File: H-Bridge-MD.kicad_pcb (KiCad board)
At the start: 2 copper layers, 85 x 50 mm, 67 parts, among them IC1 SI8650AB-B-IS1, IC2 A3921KLPTR-T, IC3 SI8650AB-B-IS1, IC4 A3921KLPTR-T, J1 Conn_01x02, J2 Conn_01x03, J3 Conn_01x05, J4 Conn_01x02, J5 Bus_mechaken_PCIexpress_x16_1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, Q1 NVMFD5C446NT1G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

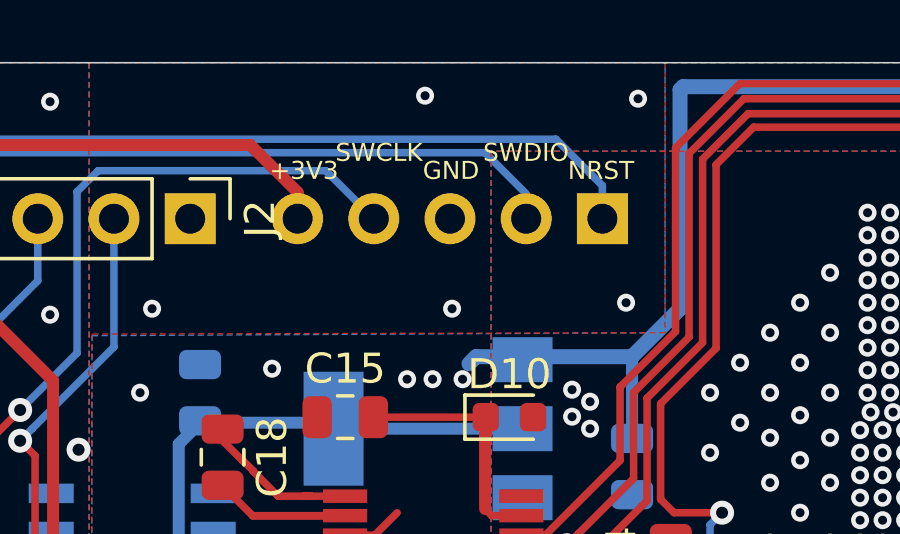
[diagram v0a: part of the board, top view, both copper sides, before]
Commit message: change
書き込み用のピンをコンスルー対応に変更
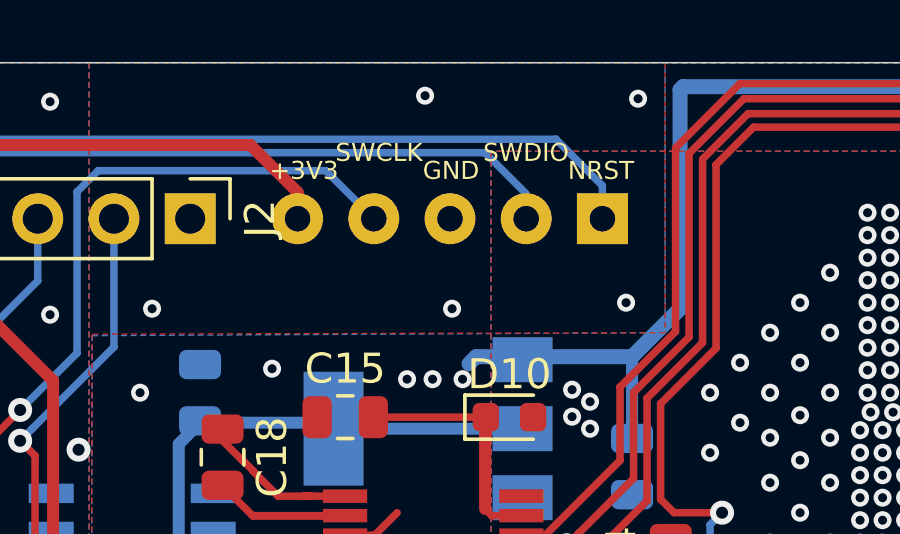
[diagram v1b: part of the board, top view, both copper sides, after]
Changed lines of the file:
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@@
     (mod_text_size 1 1)
     (mod_text_width 0.15)
-    (pad_size 3 5)
-    (pad_drill 0)
+    (pad_size 1.7 1.7)
+    (pad_drill 0.85)
     (pad_to_mask_clearance 0.051)
     (solder_mask_min_width 0.25)
@@
     (fp_line (start 1.27 1.27) (end 1.27 -11.43) (layer B.Fab) (width 0.1))
     (fp_line (start -0.635 1.27) (end 1.27 1.27) (layer B.Fab) (width 0.1))
-    (pad 5 thru_hole oval (at 0 -10.16 90) (size 1.7 1.7) (drill 1) (layers *.Cu *.Mask)
+    (pad 5 thru_hole oval (at 0 -10.16 90) (size 1.7 1.7) (drill 0.85) (layers *.Cu *.Mask)
       (net 4 +3V3))
-    (pad 4 thru_hole oval (at 0 -7.62 90) (size 1.7 1.7) (drill 1) (layers *.Cu *.Mask)
+    (pad 4 thru_hole oval (at 0 -7.62 90) (size 1.7 1.7) (drill 0.85) (layers *.Cu *.Mask)
       (net 48 /SWCLK))
-    (pad 3 thru_hole oval (at 0 -5.08 90) (size 1.7 1.7) (drill 1) (layers *.Cu *.Mask)
+    (pad 3 thru_hole oval (at 0 -5.08 90) (size 1.7 1.7) (drill 0.85) (layers *.Cu *.Mask)
       (net 1 GND))
-    (pad 2 thru_hole oval (at 0 -2.54 90) (size 1.7 1.7) (drill 1) (layers *.Cu *.Mask)
+    (pad 2 thru_hole oval (at 0 -2.54 90) (size 1.7 1.7) (drill 0.85) (layers *.Cu *.Mask)
       (net 47 /SWDIO))
-    (pad 1 thru_hole rect (at 0 0 90) (size 1.7 1.7) (drill 1) (layers *.Cu *.Mask)
+    (pad 1 thru_hole rect (at 0 0 90) (size 1.7 1.7) (drill 0.85) (layers *.Cu *.Mask)
       (net 3 NRST))
     (model ${KISYS3DMOD}/Connector_PinHeader_2.54mm.3dshapes/PinHeader_1x05_P2.54mm_Vertical.wrl
@@
   (segment (start 74.749 55.099) (end 74.75 55.1) (width 0.25) (layer F.Cu) (net 96))
   (segment (start 74.75 55.1) (end 77.833 55.1) (width 0.25) (layer F.Cu) (net 96))
-  (segment (start 78.4 73.3) (end 78.4 74.3) (width 0.25) (layer B.Cu) (net 111))
-  (segment (start 79.3 72.4) (end 78.4 73.3) (width 0.25) (layer B.Cu) (net 111))
-  (segment (start 78.4 74.3) (end 79.3 75.2) (width 0.25) (layer B.Cu) (net 111))
   (segment (start 71.374 74.7245) (end 71.3485 74.75) (width 0.25) (layer F.Cu) (net 97))
   (segment (start 71.374 71.785) (end 71.374 74.7245) (width 0.25) (layer F.Cu) (net 97))
@@
   (segment (start 77 74.85) (end 76.65 75.2) (width 0.25) (layer B.Cu) (net 110))
   (segment (start 77 72.375) (end 77 74.85) (width 0.25) (layer B.Cu) (net 110))
+  (segment (start 78.4 73.3) (end 78.4 74.3) (width 0.25) (layer B.Cu) (net 111))
+  (segment (start 79.3 72.4) (end 78.4 73.3) (width 0.25) (layer B.Cu) (net 111))
+  (segment (start 78.4 74.3) (end 79.3 75.2) (width 0.25) (layer B.Cu) (net 111))
   (segment (start 79.25 65.425) (end 79.2875 65.4625) (width 0.25) (layer B.Cu) (net 112))
   (segment (start 79.25 63.25) (end 79.25 65.425) (width 0.25) (layer B.Cu) (net 112))

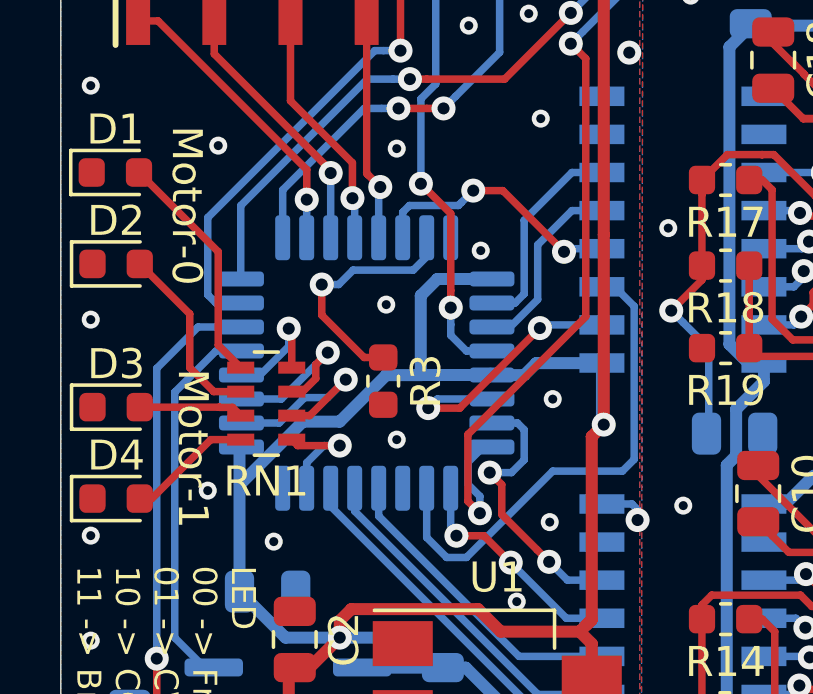
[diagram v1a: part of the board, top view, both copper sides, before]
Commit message: change
抵抗アレイを1206に変更
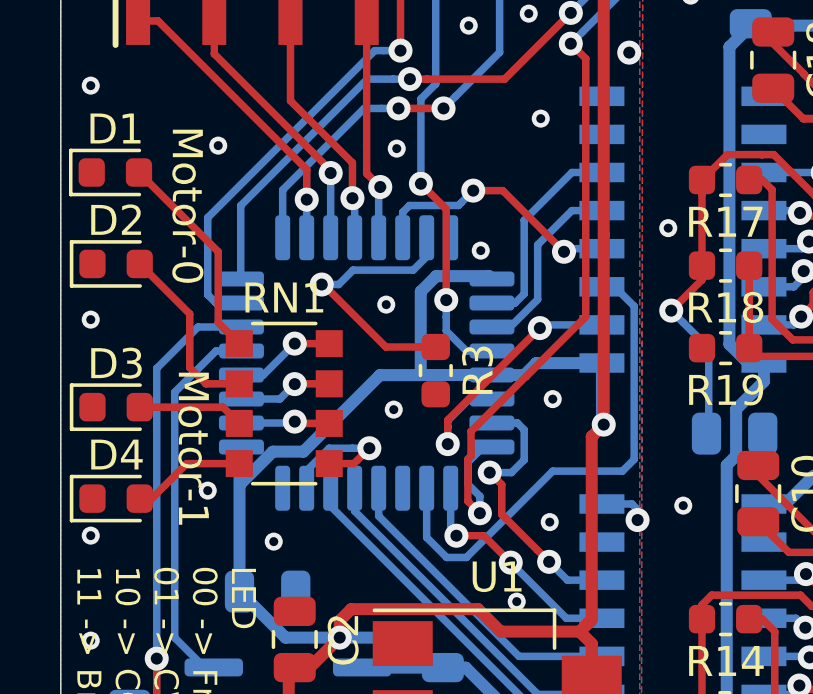
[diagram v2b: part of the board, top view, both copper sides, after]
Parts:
- R8, R9: value 10K -> 2.2K
- RN1: footprint Resistor_SMD:R_Array_Concave_4x0603 -> Resistor_SMD:R_Array_Convex_4x1206
- moved R3 1.78 mm to (62.5, 63.5)
- moved RN1 0.60 mm to (57.5, 64.6)
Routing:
- net MD1_LED_H: track 6.37 -> 2.97 mm
- net MD0_LED_L: track 6.15 -> 3.76 mm
- net /BOOT: track 8.17 -> 9.18 mm
- net Net-(D1-Pad2): track 7.91 -> 7.09 mm
- net MD1_LED_L: track 3.87 -> 4.53 mm
- net IC_RESET_0: track 9.19 -> 9.81 mm
- net MD0_LED_H: track 3.28 -> 2.74 mm

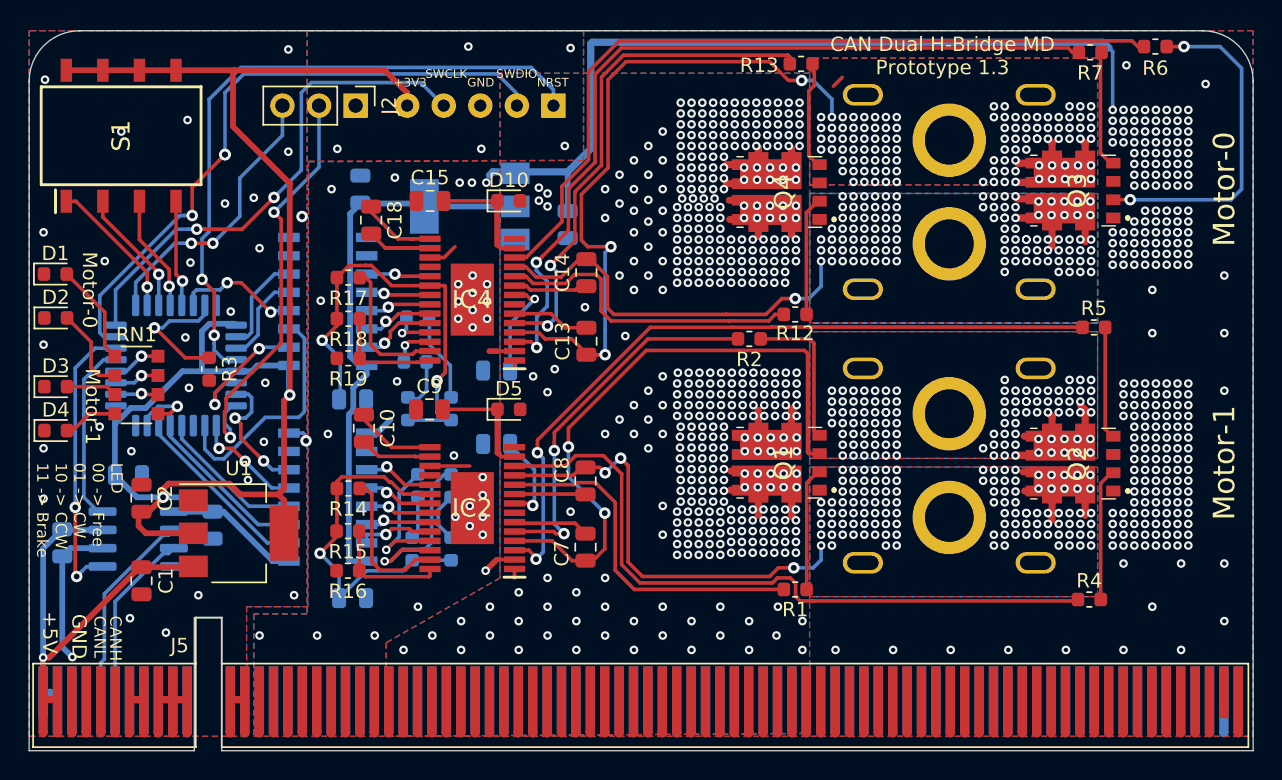
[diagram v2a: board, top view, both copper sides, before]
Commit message: change
ダイオードのフットプリントをハーフホール向けに変更
その他の微修正（主に配線）
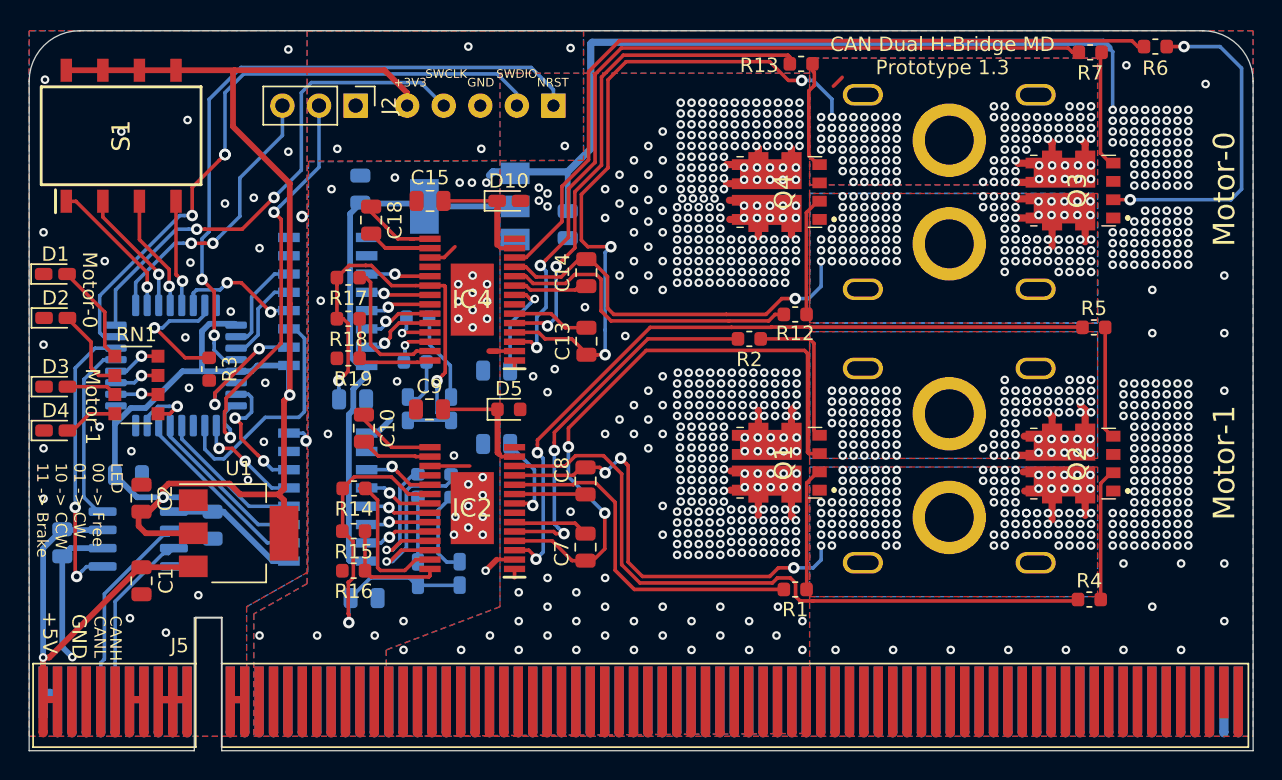
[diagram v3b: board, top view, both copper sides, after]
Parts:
- D1, D2, D3, D4, D6, D7, D8, D9: footprint LED_SMD:LED_0603_1608Metric -> LED_SMD:LED_0603_1608Metric_Castellated
- D10: footprint Diode_SMD:D_0603_1608Metric -> LED_SMD:LED_0603_1608Metric_Castellated
- moved D7 1.80 mm to (79.9, 77.7)
- moved D6 1.76 mm to (77.0, 77.7)
- moved C11 0.80 mm to (73.3, 79.4)
- moved R15 0.40 mm to (72.5, 74.8)
- moved R16 0.40 mm to (72.5, 77.5)
- moved R14 0.40 mm to (72.6, 71.8)
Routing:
- net Net-(D7-Pad1): track 3.55 -> 5.92 mm
- net V5_1: track 25.2 -> 26.9 mm
- net Net-(D6-Pad1): track 2.97 -> 4.53 mm
- net GNDPWR: vias 258 -> 260
- net VCC: vias 435 -> 432
- net GND: vias 34 -> 33

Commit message: clean
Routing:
- net VCC: vias 432 -> 461
- net GNDPWR: vias 260 -> 267

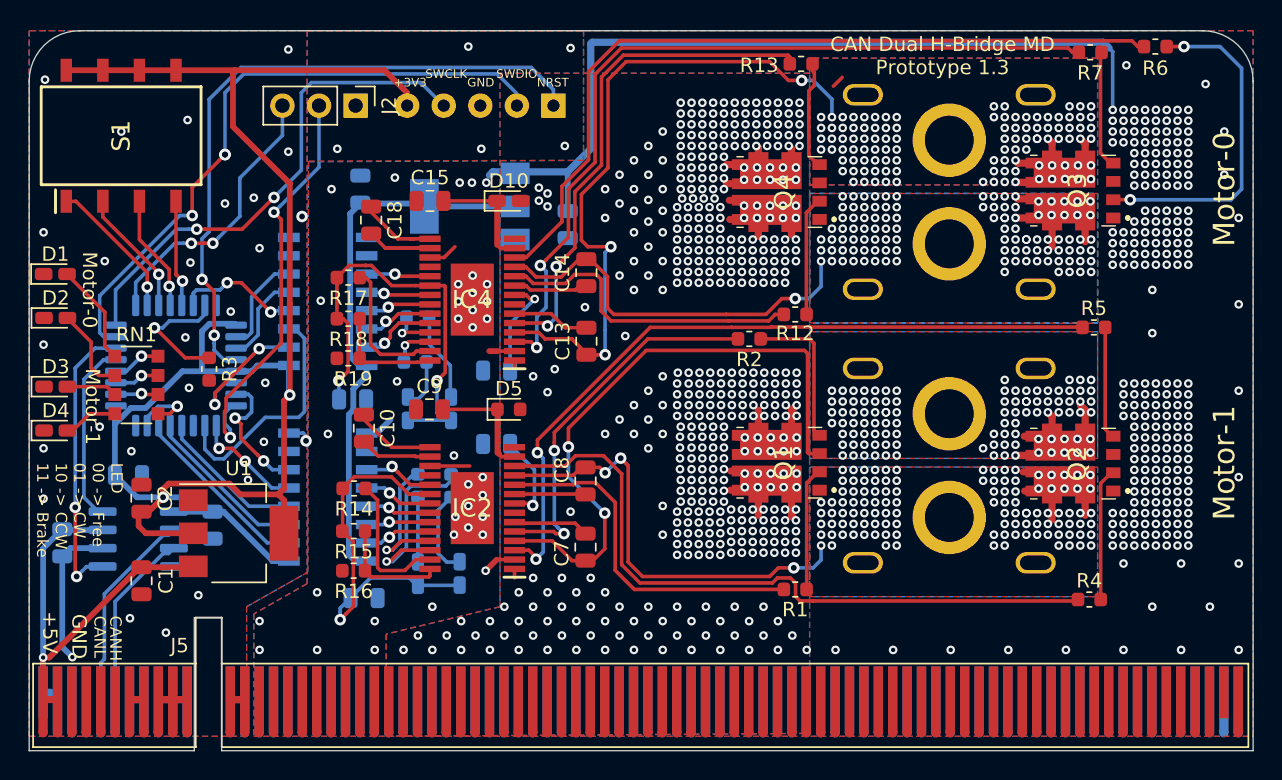
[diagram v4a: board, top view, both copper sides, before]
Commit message: change
電解コンデンサを搭載できるように配置を大幅変更
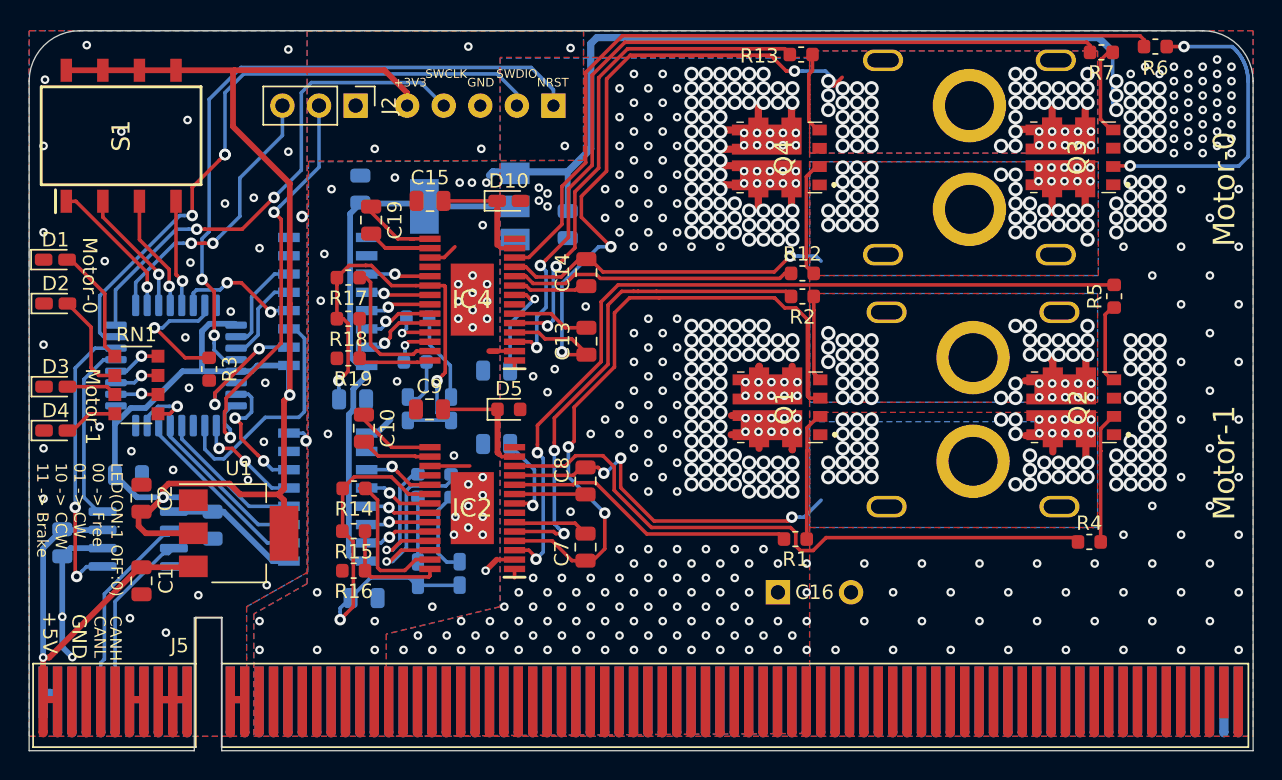
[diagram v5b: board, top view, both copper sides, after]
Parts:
- added C16: 1000u, Connector_PinSocket_2.54mm:PinSocket_1x02_P2.54mm_Vertical, F.Cu at (102.0, 79.0)
- C1: value 1uF -> 1u
- C10: value 0.47uF -> 0.47u
- C11, C15, C3, C4, C5, C9: value 0.1uF -> 0.1u
- C13, C14, C2, C6, C7, C8: value 4.7uF -> 4.7u
- C19: renamed from C18; value 0.47uF -> 0.47u
- R10, R11, R8, R9: value 2.2K -> 2.2k
- R14, R17: value 3K -> 3k
- R3: value 10K -> 10k
- RN1: value R_Pack04 -> 2.2k
- moved R2 4.72 mm to (103.7, 58.5)
- moved J1 4.23 mm to (115.5, 66.3)
- moved R4 4.00 mm to (123.6, 75.5)
- moved Q2 3.91 mm to (122.8, 66.2)
- moved Q1 3.85 mm to (102.5, 66.2)
- moved R1 3.50 mm to (103.2, 75.3)
- moved R12 2.89 mm to (103.7, 56.9)
- moved J4 2.78 mm to (115.3, 48.8)
- moved R5 2.58 mm to (125.3, 58.4), turned to 90 degrees
- moved Q4 2.40 mm to (102.4, 48.8)
- moved Q3 2.31 mm to (122.8, 48.8)
- moved D1 1.00 mm to (51.8, 55.9)
- moved D2 1.00 mm to (51.8, 58.9)
- moved R7 0.78 mm to (124.5, 41.5)
- moved R13 0.65 mm to (103.6, 41.6)
- renumbered C16 to C17, C17 to C18, C19 to C20
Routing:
- net GHB_1: track 26.4 -> 34.6 mm
- net SA_0: track 37.2 -> 30.7 mm, vias 107 -> 46
- net SA_1: track 39.5 -> 33.1 mm, vias 116 -> 45
- net GLB_1: track 51.6 -> 58.0 mm
- net GHA_1: track 24.6 -> 20.4 mm
- net GLA_1: track 48.1 -> 44.1 mm
- net Net-(Q1-Pad4): track 10.4 -> 7.04 mm
- net VCC: track 26.0 -> 23.3 mm, vias 461 -> 325
- net Net-(Q4-Pad4): track 7.99 -> 5.61 mm
- net Net-(Q2-Pad4): track 7.83 -> 5.54 mm
- net Net-(Q3-Pad4): track 8.42 -> 6.33 mm
- net SB_1: track 52.8 -> 54.8 mm, vias 103 -> 46
- net GHA_0: track 21.9 -> 19.9 mm
- net GLB_0: track 57.2 -> 58.6 mm
- net SB_0: track 58.1 -> 56.8 mm, vias 109 -> 50
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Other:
- board text added: "LED(ON:1 OFF:0) 00 -> Free 01 -> CW 10 -> CCW 11 -> Brake"
- board text removed: "LED 00 -> Free 01 -> CW 10 -> CCW 11 -> Brake"

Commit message: change
放熱ビアを1mmに変更
その他大幅な変更
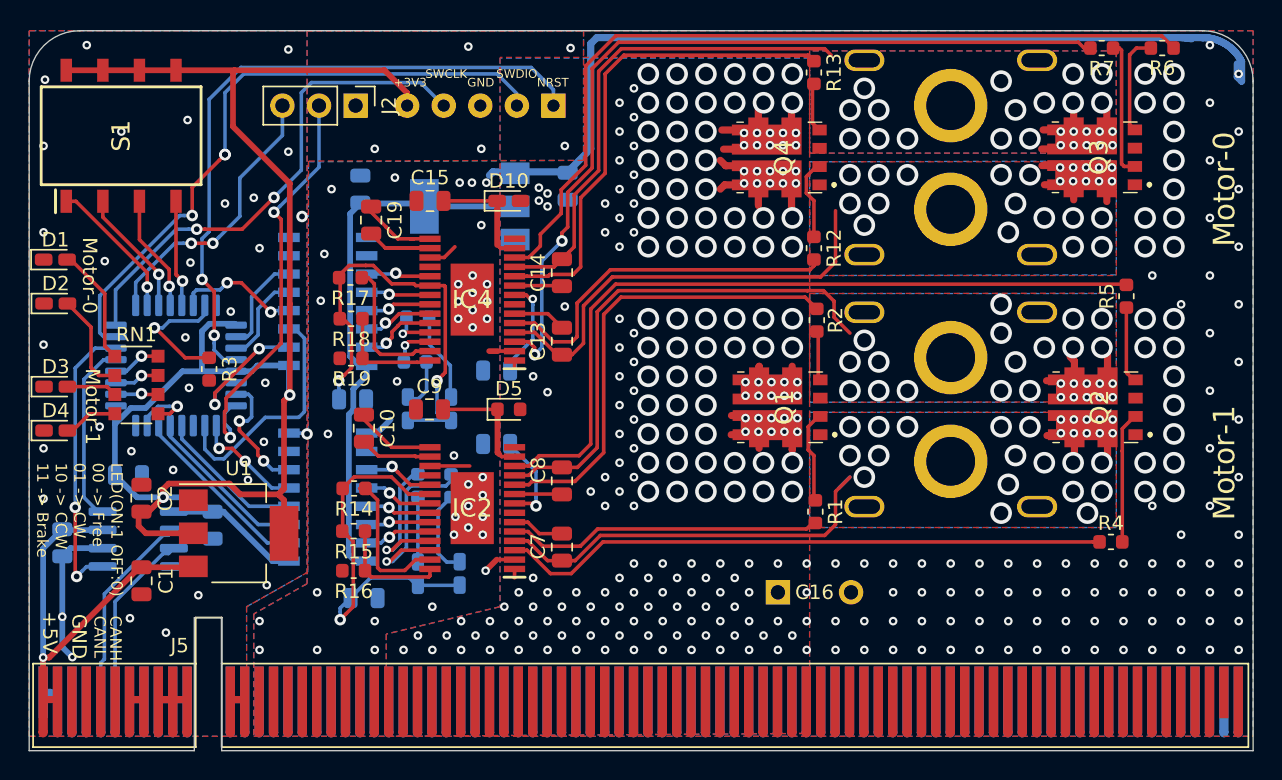
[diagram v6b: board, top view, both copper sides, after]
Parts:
- moved C17 2.66 mm to (87.4, 50.8)
- moved R1 2.35 mm to (104.6, 73.4), turned to 90 degrees
- moved R2 1.93 mm to (104.7, 60.1), turned to 90 degrees
- moved R12 1.92 mm to (104.5, 55.1), turned to 90 degrees
- moved C13 1.70 mm to (87.0, 61.6)
- moved C14 1.69 mm to (87.0, 56.8)
- moved C7 1.64 mm to (87.0, 75.9)
- moved C8 1.64 mm to (87.0, 71.3)
- moved J1 1.55 mm to (114.0, 66.3)
- moved R13 1.53 mm to (104.5, 42.9), turned to 90 degrees
- moved Q2 1.50 mm to (124.3, 66.2)
- moved Q3 1.50 mm to (124.3, 48.8)
- moved R4 1.50 mm to (125.1, 75.5)
- moved J4 1.30 mm to (114.0, 48.8)
- moved R5 0.85 mm to (126.2, 58.4)
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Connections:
- J1 pad 1: SB_1 -> SA_1
- J1 pad 2: SA_1 -> SB_1
- J4 pad 1: SB_0 -> SA_0
- J4 pad 2: SA_0 -> SB_0
- Q1 pad 1: SA_1 -> SB_1
- Q1 pad 3: SB_1 -> SA_1
- Q2 pad 5: SB_1 -> SA_1
- Q2 pad 6: SA_1 -> SB_1
- Q3 pad 5: SB_0 -> SA_0
- Q3 pad 6: SA_0 -> SB_0
- Q4 pad 1: SA_0 -> SB_0
- Q4 pad 3: SB_0 -> SA_0
- R1 pad 1: GHA_1 -> GHB_1
- R12 pad 1: GHA_0 -> GHB_0
- R13 pad 2: GHB_0 -> GHA_0
- R2 pad 2: GHB_1 -> GHA_1
- R4 pad 1: GLA_1 -> GLB_1
- R5 pad 2: GLB_1 -> GLA_1
- R6 pad 2: Net-(Q3-Pad2) -> Net-(Q3-Pad4)
- R7 pad 1: Net-(Q3-Pad4) -> Net-(Q3-Pad2)
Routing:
- net SB_0: track 56.8 -> 34.7 mm, vias 50 -> 25
- net SB_1: track 54.8 -> 36.0 mm, vias 46 -> 27
- net GLB_1: track 58.0 -> 42.6 mm, vias 2 -> 0
- net GHA_0: track 19.9 -> 34.2 mm
- net GHB_1: track 34.6 -> 21.8 mm, vias 2 -> 0
- net Net-(Q3-Pad2): track 22.1 -> 9.55 mm, vias 2 -> 0
- net GHA_1: track 20.4 -> 32.3 mm
- net SA_1: track 33.1 -> 44.1 mm, vias 45 -> 26
- net GHB_0: track 35.3 -> 25.3 mm, vias 2 -> 0
- net SA_0: track 30.7 -> 40.4 mm, vias 46 -> 25
- net GLA_1: track 44.1 -> 53.2 mm
- net GNDPWR: track 69.7 -> 75.6 mm, vias 194 -> 140
- net Net-(Q1-Pad4): track 7.04 -> 3.46 mm
- net Net-(Q1-Pad2): track 9.01 -> 6.44 mm
- net Net-(Q4-Pad2): track 8.16 -> 5.61 mm
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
